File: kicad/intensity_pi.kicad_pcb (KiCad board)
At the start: 4 copper layers, 87.5 x 171.2 mm, 130 parts, among them J1 Input A, J2 Input B / Setpoint, J3 Monitor, J4 Output, J7 select 1, J8 Screw_Terminal_01x03, Q1 2N7002E, Q2 2N7002E, SW1 SW_SPDT, SW2 SW_SPDT, SW3 SW_SPDT, SW5 EG6100-ND, U1 LM4040DBZ-5, U10 OPA189, U11 PC817, U12 OPA189, U13 BUF634A, U14 TMUX6123, U17 TMUX6123, U18 OPA189, U19 L7815, U2 LM4040DBZ-5, U20 OPA189, U21 OPA189, U22 4x Comparator, U23 L7915, U3 INA849, U4 INA849, U5 OPA189, U6 LM2937-5, U7 OPA189, U8 BUF634A, U9 LM317_TO-252

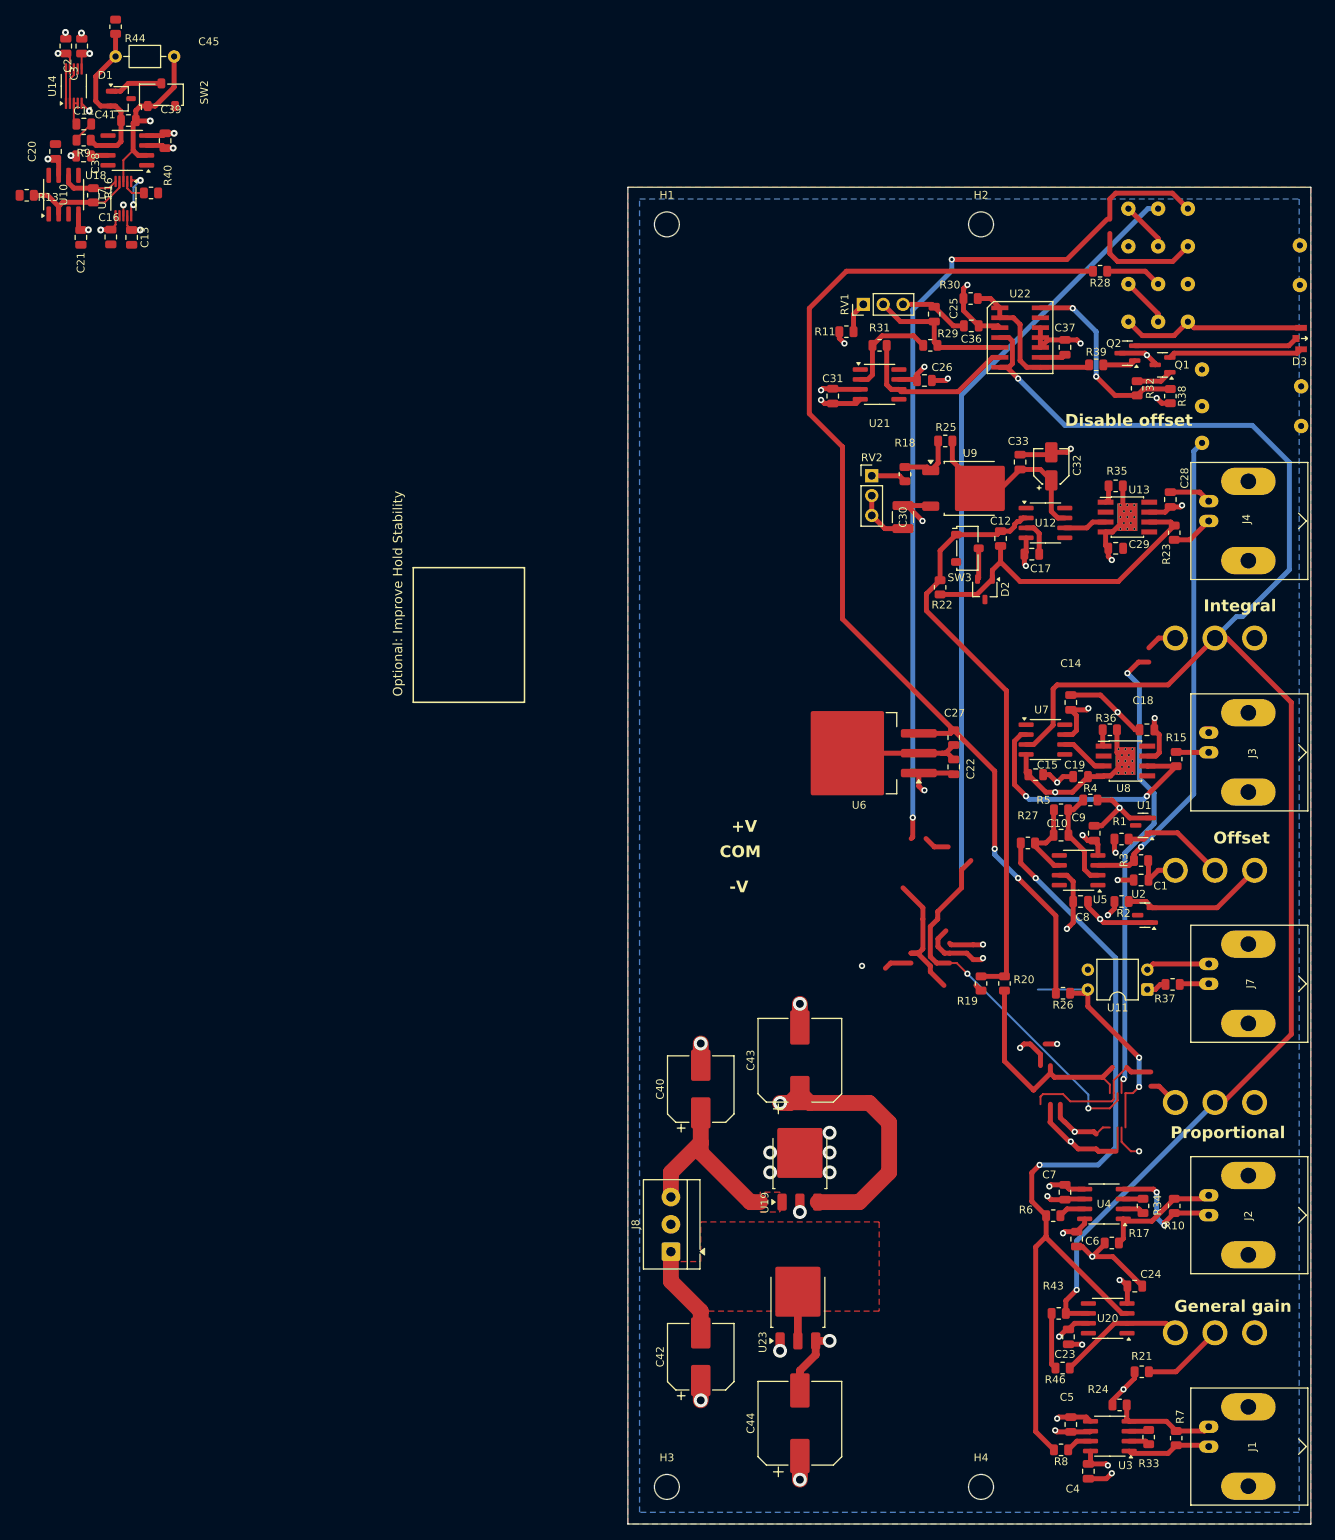
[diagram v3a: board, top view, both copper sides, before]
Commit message: Condensed Layout, Removed 5V supply, Shortened Board
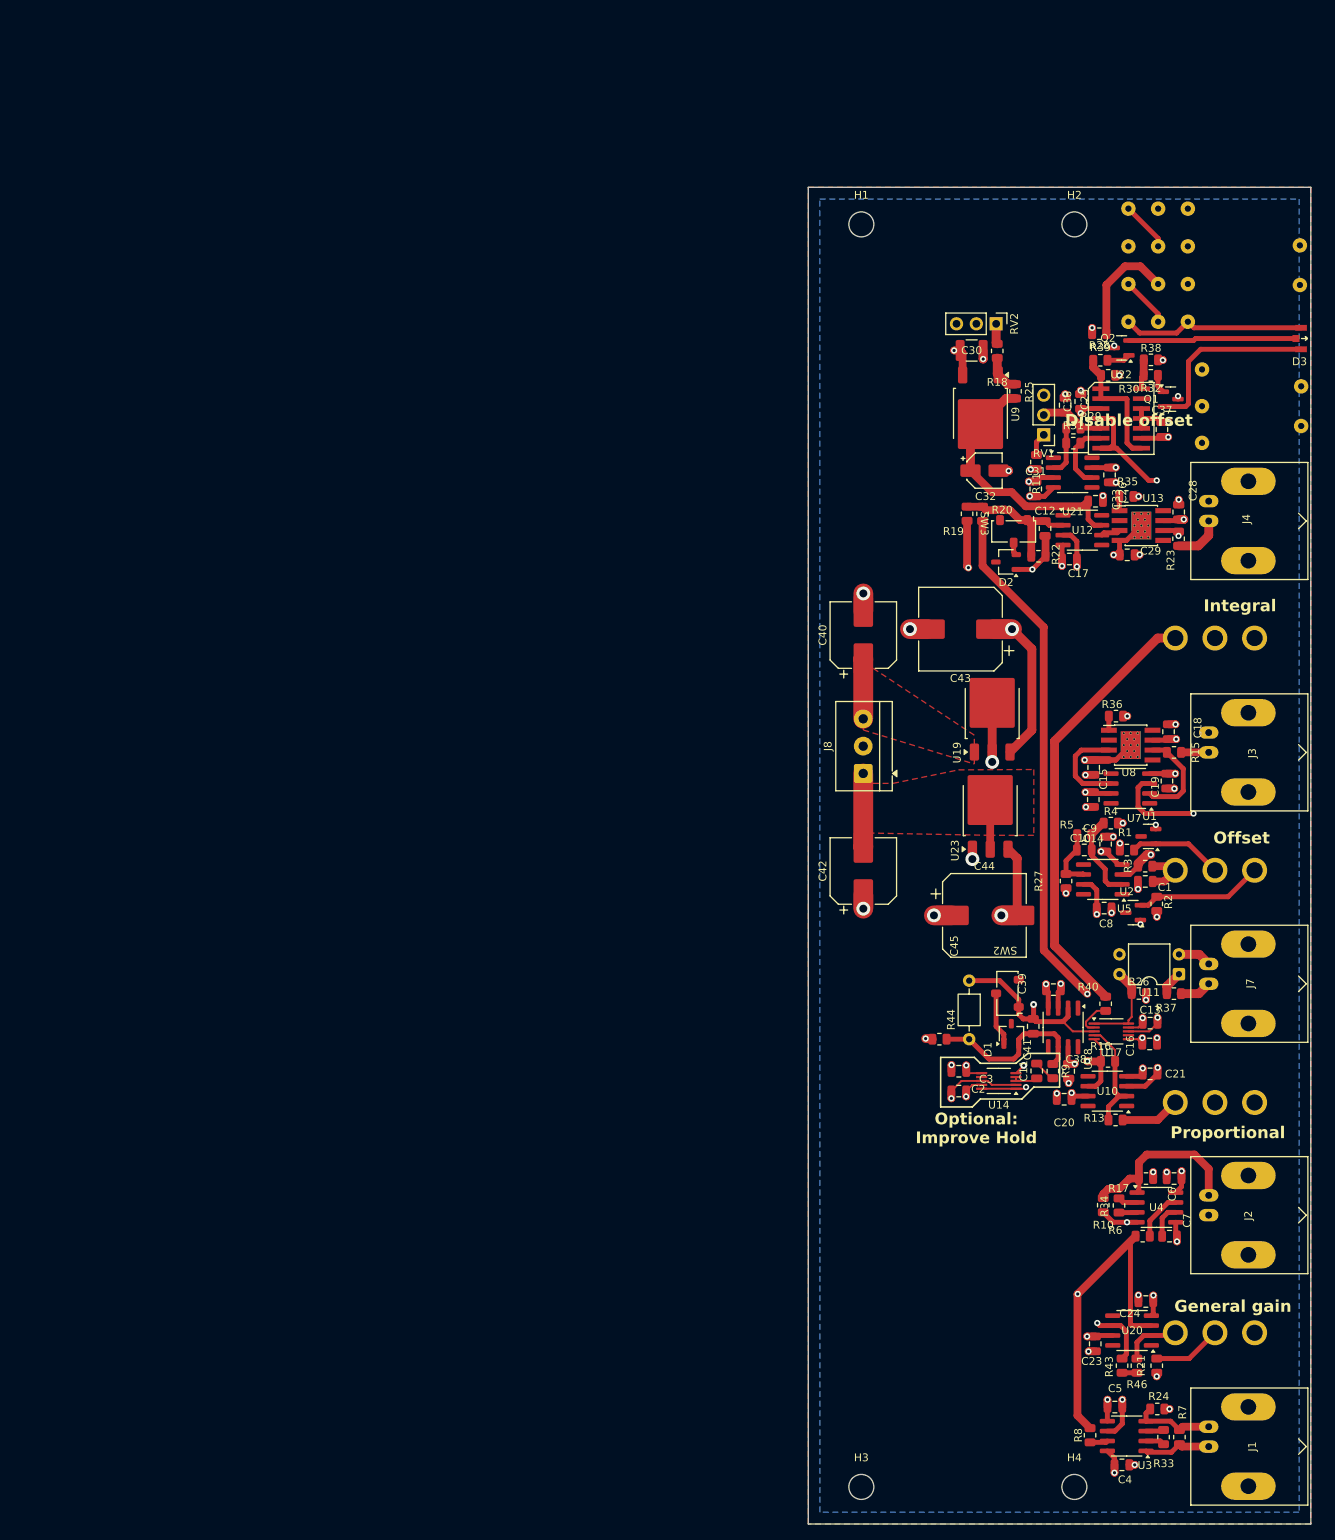
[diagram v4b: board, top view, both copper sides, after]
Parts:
- removed C22: 0.1uF, Capacitor_SMD:C_0805_2012Metric
- removed C27: 10uF, Capacitor_SMD:C_0805_2012Metric
- removed U6: LM2937-5, Package_TO_SOT_SMD:TO-263-3_TabPin2
- R28: value 180 -> 1k
- moved R13 183.0 mm to (233.5, 101.2), turned to 180 degrees
- moved C20 177.3 mm to (226.9, 98.6), turned to 180 degrees
- moved U10 176.3 mm to (232.4, 97.5), turned to 180 degrees
- moved C2 176.1 mm to (213.4, 97.5), turned to 180 degrees
- moved U14 174.0 mm to (218.5, 96.2), turned to 180 degrees
- moved C21 173.9 mm to (237.9, 95.3), turned to 180 degrees
- moved C3 172.8 mm to (213.4, 95.0), turned to 0 degrees
- moved C38 172.3 mm to (227.5, 95.0), turned to -90 degrees
- moved R9 172.2 mm to (225.4, 95.0), turned to -90 degrees
- moved C11 172.1 mm to (223.4, 95.0), turned to 90 degrees
- moved R16 170.9 mm to (232.5, 93.7), turned to 180 degrees
- moved C16 168.5 mm to (237.9, 91.5), turned to 180 degrees
- moved R44 167.2 mm to (210.9, 90.9), turned to 0 degrees
- moved U17 165.5 mm to (232.9, 89.9), turned to 0 degrees
- moved D1 165.4 mm to (220.1, 90.2), turned to 90 degrees
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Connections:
- R26 pad 1: +5V -> +15V
- R28 pad 1: +5V -> +15V
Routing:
- net +5V: track 143.8 -> 0.00 mm, vias 2 -> 0
- net Net-(R44-Pad1): track 13.8 -> 119.9 mm, vias 0 -> 1
- net GND: track 184.4 -> 85.7 mm, vias 35 -> 45
- net Error_signal: track 214.0 -> 154.7 mm, vias 2 -> 3
- net +15V: track 128.6 -> 69.6 mm, vias 20 -> 21
- net Net-(R40-Pad2): track 63.5 -> 4.74 mm, vias 2 -> 0
- net Net-(SW3-A): track 75.5 -> 18.2 mm
- net Net-(R12-Pad2): track 3.90 -> 56.4 mm
- net Net-(R16-Pad2): track 37.1 -> 84.2 mm, vias 0 -> 2
- net -15V: track 104.3 -> 64.1 mm, vias 17 -> 18
- net Net-(SW2-A): track 182.3 -> 145.1 mm, vias 4 -> 2
- net Net-(U7--): track 34.5 -> 12.5 mm, vias 2 -> 0
- net Net-(R32-Pad2): track 25.0 -> 3.82 mm, vias 2 -> 0
- net Net-(U10--): track 33.4 -> 14.2 mm
- net +V_DC_unregulated: track 23.9 -> 7.69 mm
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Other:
- board size 87.5 x 171.2 mm -> 64.4 x 171.2 mm
- board text added: "Optional: Improve Hold"
- board text removed: "+V"
- board text removed: "-V"
- board text removed: "COM"
- board text removed: "Optional: Improve Hold Stability"

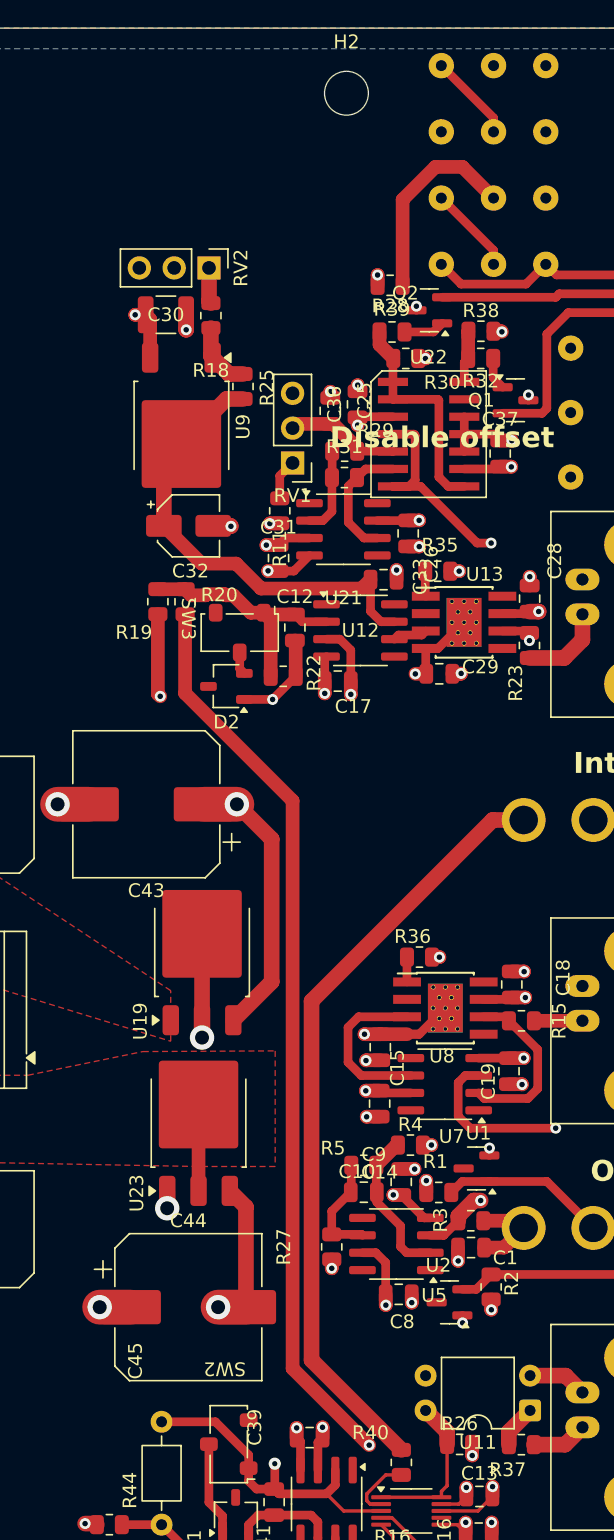
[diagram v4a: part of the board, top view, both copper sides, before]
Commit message: Further improvements to layout, reduce potential for crosstalk
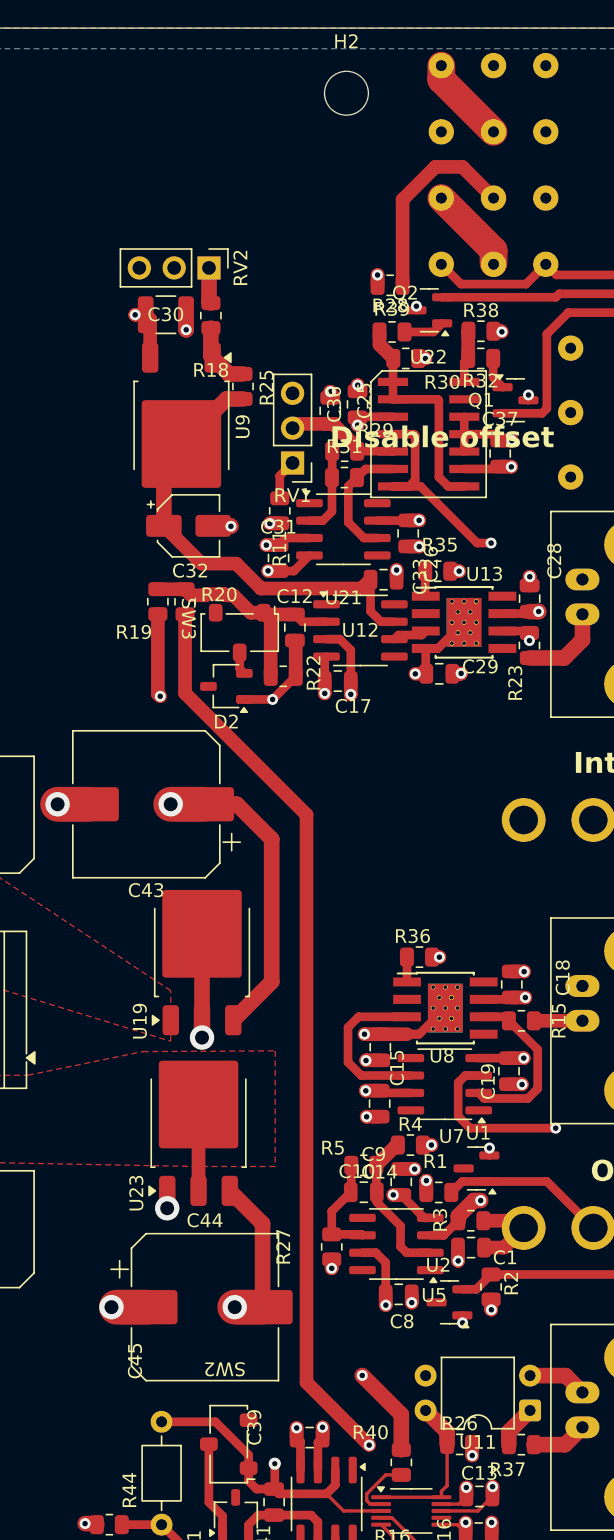
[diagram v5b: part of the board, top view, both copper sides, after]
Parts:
- moved C44 1.21 mm to (217.9, 75.0)
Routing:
- net Net-(R12-Pad2): track 56.4 -> 52.0 mm, vias 0 -> 1
- net Net-(R44-Pad1): track 119.9 -> 123.0 mm
- net Net-(SW2-A): track 145.1 -> 148.0 mm
- net +15V: track 69.6 -> 72.0 mm
- net Net-(D1-A): track 151.0 -> 152.3 mm
- net -15V: track 64.1 -> 64.6 mm

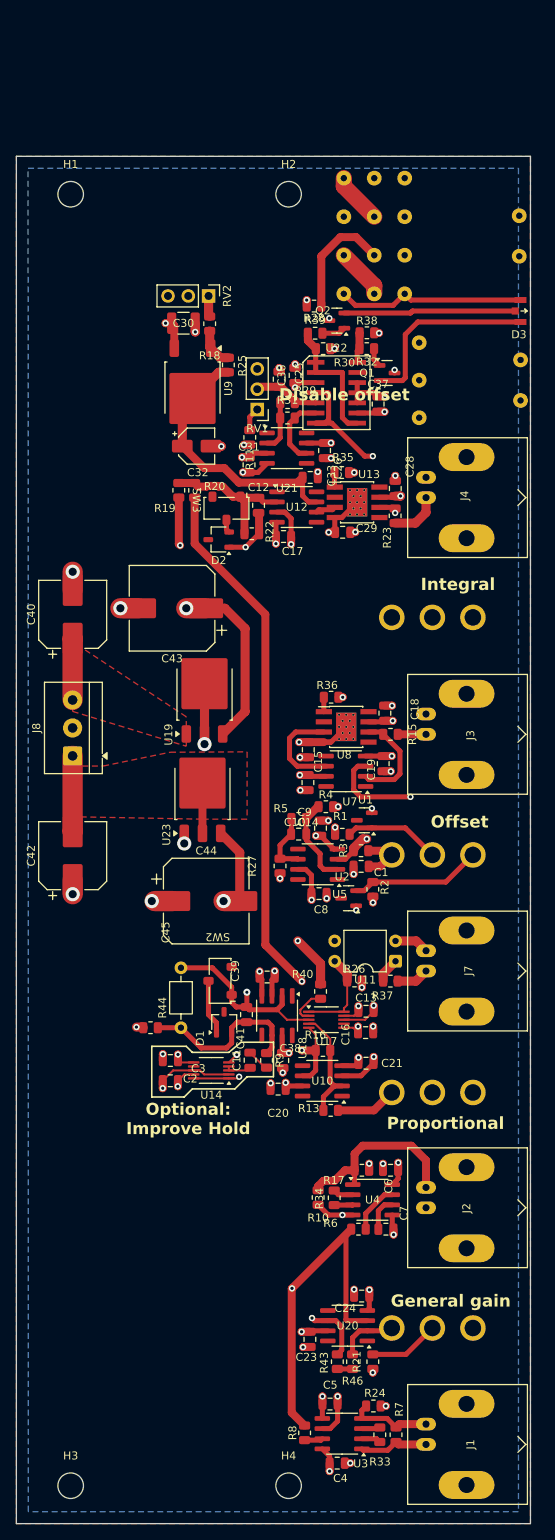
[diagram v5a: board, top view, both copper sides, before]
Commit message: Rearranged Edge Componenets, simpler board, wider but shorter depth
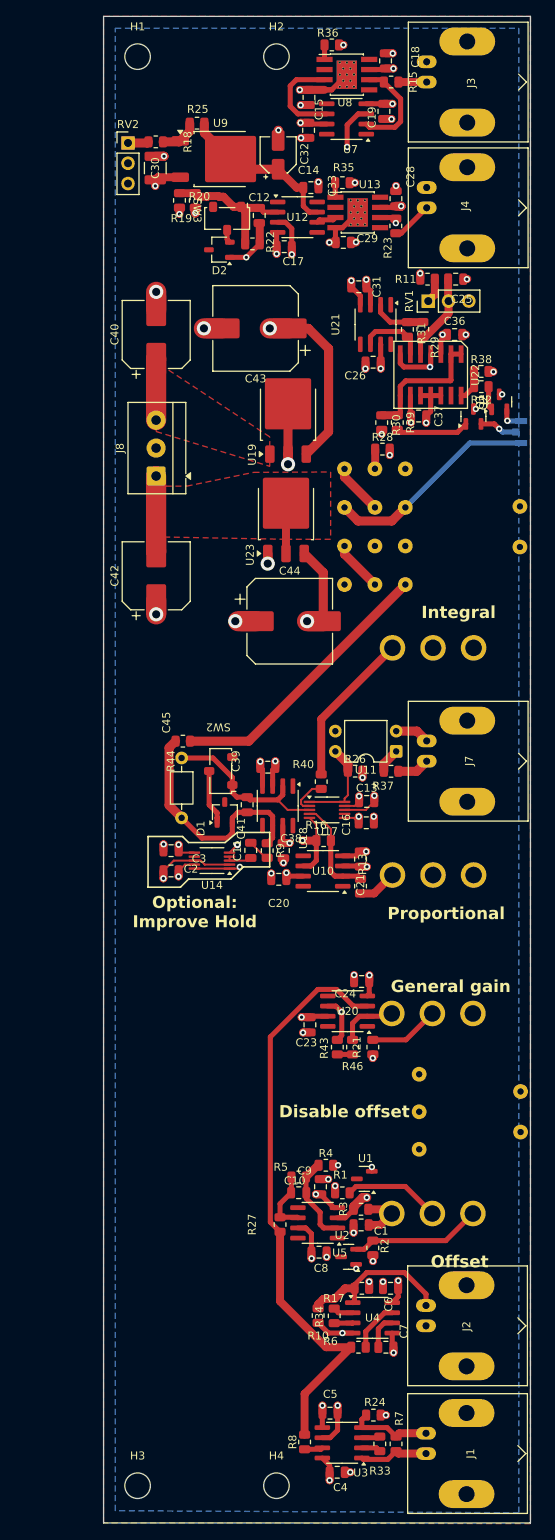
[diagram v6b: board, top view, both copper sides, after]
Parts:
- D3: moved to B.Cu
- moved SW1 91.6 mm to (244.6, 101.4)
- moved C19 81.7 mm to (240.1, -23.9)
- moved J3 81.7 mm to (245.5, -27.6)
- moved U7 81.7 mm to (235.5, -22.9)
- moved C14 81.7 mm to (230.7, -21.5)
- moved C15 81.7 mm to (230.8, -25.6)
- moved C18 81.7 mm to (240.4, -30.2)
- moved R15 81.7 mm to (241.1, -27.5)
- moved R36 81.7 mm to (233.6, -32.2)
- moved U8 81.7 mm to (235.5, -28.5)
- moved C9 44.9 mm to (232.2, 110.8)
- moved C1 44.9 mm to (237.3, 115.6)
- moved C10 44.9 mm to (229.5, 111.6)
- moved C8 44.9 mm to (232.0, 119.0)
- moved R1 44.9 mm to (234.9, 111.6)
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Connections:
- SW5 pad 1: Net-(D1-A) -> unconnected-(SW5-Pad1)
- SW5 pad 10: Net-(D3-A) -> Net-(R44-Pad1)
- SW5 pad 12: Net-(D3-A) -> unconnected-(SW5-Pad12)
- SW5 pad 2: Net-(SW2-A) -> Net-(R28-Pad2)
- SW5 pad 4: Net-(R44-Pad1) -> Net-(D3-A)
- SW5 pad 6: unconnected-(SW5-Pad6) -> Net-(D3-A)
- SW5 pad 7: unconnected-(SW5-Pad7) -> Net-(D1-A)
- SW5 pad 8: Net-(R28-Pad2) -> Net-(SW2-A)
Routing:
- net Net-(R44-Pad1): track 123.0 -> 35.1 mm, vias 1 -> 0
- net Net-(SW2-A): track 148.0 -> 75.2 mm, vias 2 -> 1
- net Net-(SW1-A): track 60.5 -> 14.0 mm
- net Net-(R12-Pad2): track 52.0 -> 19.5 mm, vias 1 -> 0
- net Net-(U20-+): track 97.6 -> 73.7 mm, vias 2 -> 0
- net Net-(D3-K1): track 23.9 -> 3.20 mm, vias 0 -> 1
- net Net-(D1-A): track 152.3 -> 133.0 mm
- net Net-(D3-K2): track 21.5 -> 4.80 mm, vias 0 -> 1
- net Vlim+: track 32.1 -> 19.0 mm
- net Net-(R28-Pad2): track 14.8 -> 2.44 mm
- net Net-(R16-Pad2): track 84.2 -> 96.5 mm
- net Error_signal: track 154.7 -> 142.6 mm
- net Net-(Q2-G): track 3.01 -> 9.16 mm
- net Net-(U14C-SEL1): track 36.8 -> 40.4 mm
- net Net-(D3-A): track 23.6 -> 26.9 mm
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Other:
- board size 64.4 x 171.2 mm -> 53.5 x 188.7 mm

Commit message: Further Layout Refinements
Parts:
- moved R44 19.3 mm to (232.7, 47.2)
- moved C41 16.5 mm to (227.1, 47.0), turned to 180 degrees
- moved C38 16.2 mm to (227.0, 52.5), turned to 0 degrees
- moved C3 13.1 mm to (224.5, 61.7), turned to -90 degrees
- moved C2 12.8 mm to (222.0, 61.7), turned to 90 degrees
- moved R9 12.3 mm to (217.7, 59.2)
- moved C45 11.2 mm to (223.3, 49.8), turned to 0 degrees
- moved C11 8.59 mm to (219.7, 61.0)
- moved D1 6.53 mm to (223.3, 58.2), turned to 0 degrees
- moved U18 5.87 mm to (228.3, 57.4), turned to 90 degrees
- moved SW2 5.81 mm to (222.3, 53.6), turned to -90 degrees
- moved U14 5.63 mm to (223.3, 66.8), turned to 90 degrees
- moved C39 4.59 mm to (227.9, 62.2), turned to 0 degrees
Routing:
- net Net-(D1-A): track 133.0 -> 106.4 mm, vias 1 -> 3
- net Net-(R44-Pad1): track 35.1 -> 15.7 mm
- net Net-(SW2-A): track 75.2 -> 58.1 mm, vias 1 -> 2
- net GND: track 82.6 -> 94.0 mm
- net Net-(C11-Pad1): track 2.83 -> 12.6 mm
- net Net-(U14C-SEL1): track 40.4 -> 34.1 mm
- net Net-(D1-K): track 6.92 -> 2.37 mm
- net +15V: track 72.2 -> 73.2 mm
- net Net-(R16-Pad2): track 96.5 -> 95.7 mm
- net Net-(C11-Pad2): track 2.66 -> 2.07 mm
- net -15V: track 64.8 -> 65.4 mm
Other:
- board text removed: "Optional: Improve Hold"
